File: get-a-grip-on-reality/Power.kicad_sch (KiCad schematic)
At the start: 16 parts, among them J1 Battery Connector, J4 Conn_01x05_Pin, U2 BQ25887

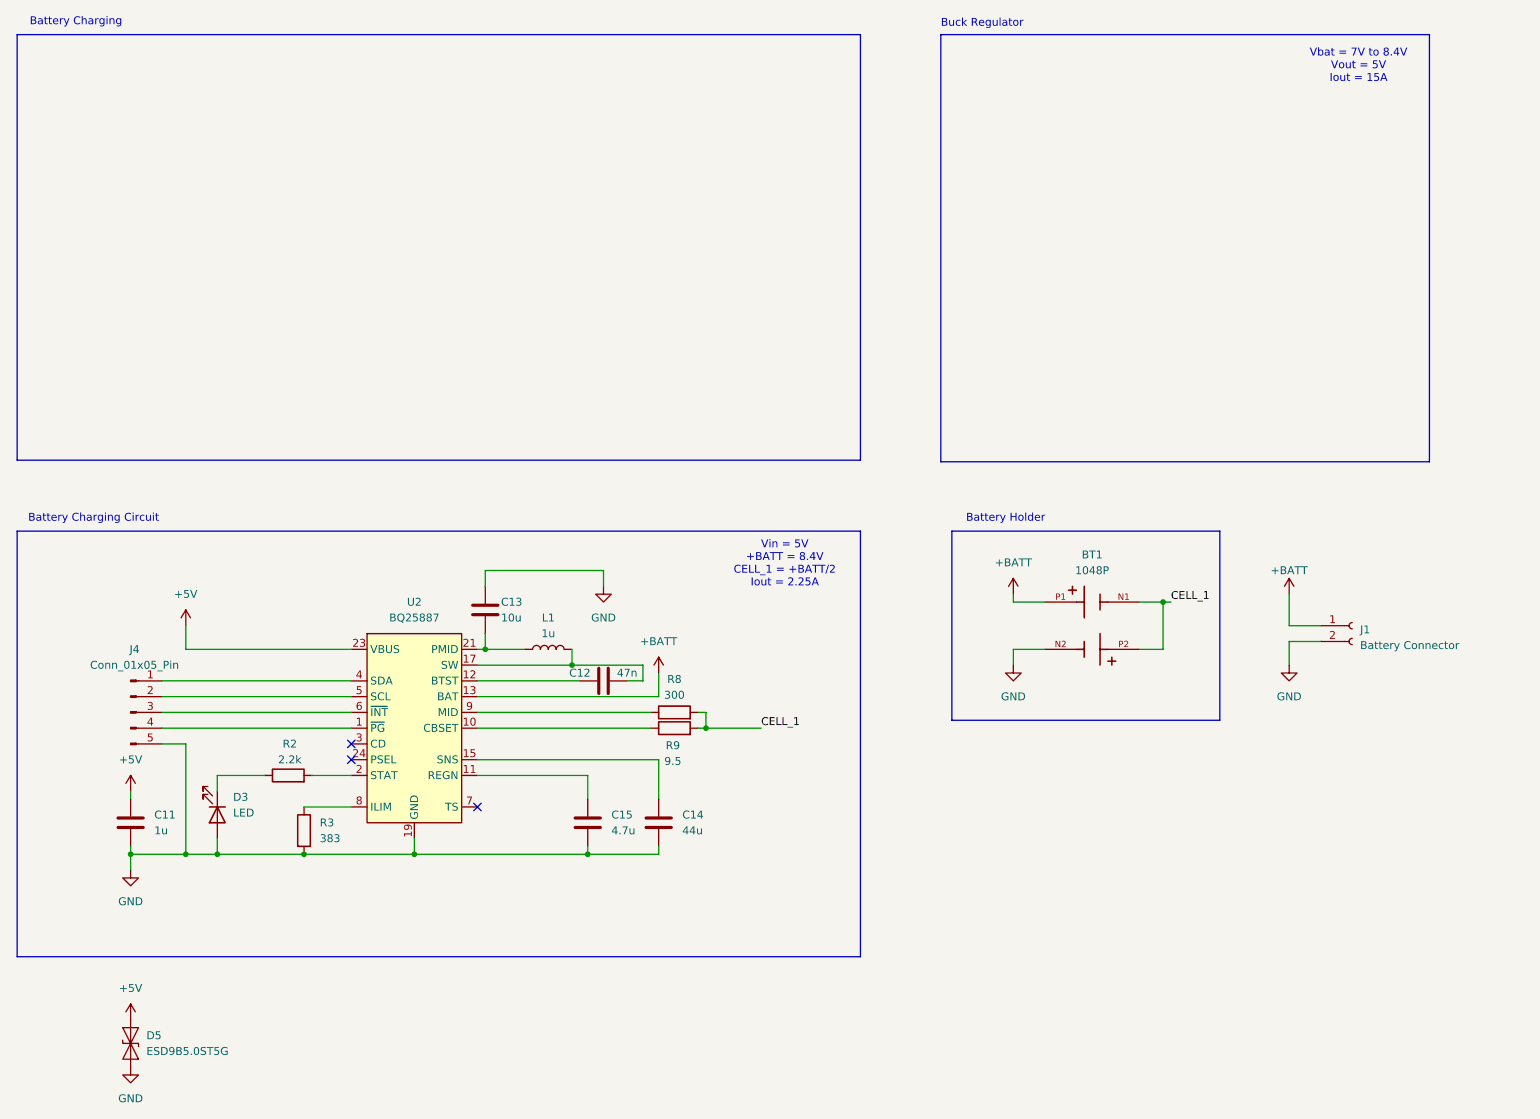
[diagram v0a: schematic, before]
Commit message: finish mcu and power page
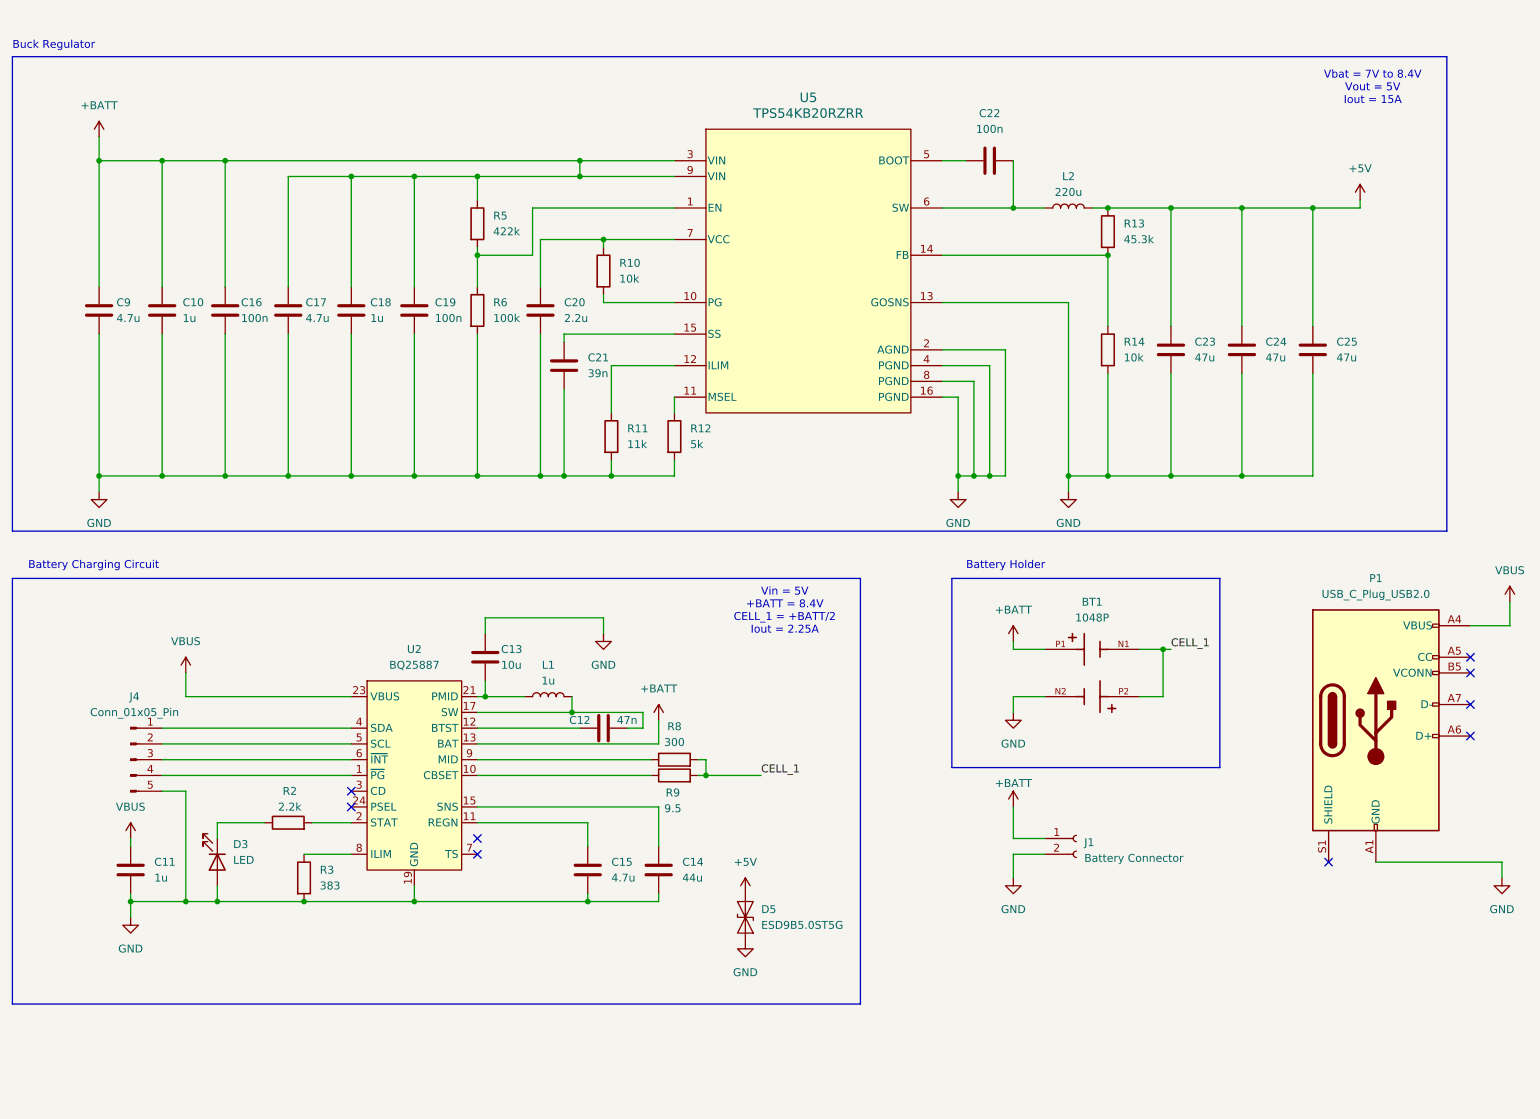
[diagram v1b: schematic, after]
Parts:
- added C10, C18: 1u, symbol Device:C
- added C16, C19, C22: 100n, symbol Device:C
- added C17, C9: 4.7u, symbol Device:C
- added C20: 2.2u, symbol Device:C
- added C21: 39n, symbol Device:C
- added C23, C24, C25: 47u, symbol Device:C
- added L2: 220u, symbol Device:L
- added P1: USB_C_Plug_USB2.0, symbol Connector:USB_C_Plug_USB2.0
- added R10, R14: 10k, symbol Device:R
- added R11: 11k, symbol Device:R
- added R12: 5k, symbol Device:R
- added R13: 45.3k, symbol Device:R
- added R5: 422k, symbol Device:R
- added R6: 100k, symbol Device:R
- added U5: TPS54KB20RZRR, RZR0016A-MFG, symbol 2024-06-26_16-50-44:TPS54KB20RZRR
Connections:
- net +5V: now also C23.1, C24.1, C25.1, L2.2, R13.1; no longer C11.1, U2.23 (VBUS)
- net +BATT: now also C10.1, C16.1, C17.1, C18.1, C19.1, C9.1, R5.1, U5.3 (VIN), U5.9 (VIN)
- net GND: now also C10.2, C16.2, C17.2, C18.2, C19.2, C20.2, C21.2, C23.2, C24.2, C25.2, C9.2, P1.A1 (GND), P1.A12 (GND), P1.B1 (GND), P1.B12 (GND), R11.2, R12.2, R14.2, R6.2, U5.13 (GOSNS), U5.16 (PGND), U5.2 (AGND), U5.4 (PGND), U5.8 (PGND)
- new net: C21.1, U5.15 (SS)
- new net: R12.1, U5.11 (MSEL)
- new net: C22.2, L2.1, U5.6 (SW)
- new net: R11.1, U5.12 (ILIM)
- new net: R5.2, R6.1, U5.1 (EN)
- new net: C22.1, U5.5 (BOOT)
- new net: C20.1, R10.1, U5.7 (VCC)
- new net: R10.2, U5.10 (PG)
- new net: R13.2, R14.1, U5.14 (FB)
- new net VBUS: C11.1, P1.A4 (VBUS), P1.A9 (VBUS), P1.B4 (VBUS), P1.B9 (VBUS), U2.23 (VBUS)
- no-connect marks 3 -> 9
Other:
- note removed: "Battery Charging"
- moved on the sheet: BT1, C11, C12, C13, C14, C15, D3, J1, J4, L1, R2, R3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

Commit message: add output
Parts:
- removed P1: USB_C_Plug_USB2.0, symbol Connector:USB_C_Plug_USB2.0
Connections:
- no-connect marks 9 -> 4

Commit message: add more to pcb
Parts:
- BT1: footprint 1048P:BAT_1048P -> fydp library:BAT_1048P
- C12: renamed from C11; footprint (none) -> Capacitor_SMD:C_0805_2012Metric
- C13: renamed from C9; footprint (none) -> Capacitor_SMD:C_0805_2012Metric
- C14: renamed from C10; footprint (none) -> Capacitor_SMD:C_0805_2012Metric
- C15: renamed from C16; footprint (none) -> Capacitor_SMD:C_0805_2012Metric
- C16: renamed from C17; footprint (none) -> Capacitor_SMD:C_0805_2012Metric
- C17: renamed from C18; footprint (none) -> Capacitor_SMD:C_0805_2012Metric
- C18: renamed from C19; footprint (none) -> Capacitor_SMD:C_0805_2012Metric
- C19: renamed from C13; footprint (none) -> Capacitor_SMD:C_0805_2012Metric
- C20, C21: footprint (none) -> Capacitor_SMD:C_0805_2012Metric
- C22: renamed from C15; footprint (none) -> Capacitor_SMD:C_0805_2012Metric
- C23: renamed from C12; footprint (none) -> Capacitor_SMD:C_0805_2012Metric
- C24: renamed from C14; footprint (none) -> Capacitor_SMD:C_0805_2012Metric
- C25: renamed from C22; footprint (none) -> Capacitor_SMD:C_0805_2012Metric
- C26: renamed from C23; footprint (none) -> Capacitor_SMD:C_0805_2012Metric
- C27: renamed from C24; footprint (none) -> Capacitor_SMD:C_0805_2012Metric
- C28: renamed from C25; footprint (none) -> Capacitor_SMD:C_0805_2012Metric
- D4: renamed from D3; footprint (none) -> LED_SMD:LED_0805_2012Metric
- J13: renamed from J4; footprint (none) -> Connector_PinHeader_2.54mm:PinHeader_1x05_P2.54mm_Vertical
- J14: renamed from J1; value Battery Connector -> Battery Connector Bat; footprint Connector_JST:JST_PH_S2B-PH-K_1x02_P2.00mm_Horizontal -> Connector_AMASS:AMASS_XT30PW-F_1x02_P2.50mm_Horizontal
- L1: footprint (none) -> Inductor_SMD:L_Taiyo-Yuden_MD-2020
- L2: footprint (none) -> Inductor_SMD:L_Bourns_SRU5016_5.2x5.2mm
- R10: renamed from R12; footprint (none) -> Resistor_SMD:R_0805_2012Metric
- R11: renamed from R8; footprint (none) -> Resistor_SMD:R_0805_2012Metric
- R12: renamed from R9; footprint (none) -> Resistor_SMD:R_0805_2012Metric
- R13, R14: footprint (none) -> Resistor_SMD:R_0805_2012Metric
- R4: renamed from R2; footprint (none) -> Resistor_SMD:R_0805_2012Metric
- R5: renamed from R3; footprint (none) -> Resistor_SMD:R_0805_2012Metric
- R6: renamed from R5; footprint (none) -> Resistor_SMD:R_0805_2012Metric
- R7: renamed from R6; footprint (none) -> Resistor_SMD:R_0805_2012Metric
- R8: renamed from R10; footprint (none) -> Resistor_SMD:R_0805_2012Metric
- R9: renamed from R11; footprint (none) -> Resistor_SMD:R_0805_2012Metric
- U6: renamed from U5; footprint RZR0016A-MFG -> fydp library:RZR0016A-MFG
- renumbered U2 to U5
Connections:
- net +5V: now also J14.1 (Pin_1)
- net +BATT: no longer J14.1 (Pin_1)
- net at J13.1 (Pin_1): now also U5.1 (~{PG}); no longer U5.4 (SDA)
- net at J13.2 (Pin_2): now also U5.4 (SDA); no longer U5.5 (SCL)
- net at J13.3 (Pin_3): now also U5.5 (SCL); no longer U5.6 (~{INT})
- net at J13.4 (Pin_4): now also U5.6 (~{INT}); no longer U5.1 (~{PG})
- net SW_5: now reaches C25.2, L2.1, U6.6 (SW)
- net SNS: now reaches C24.1, U5.15 (SNS), U5.16 (SNS)
- net SW_BAT: now reaches C23.2, L1.2, U5.17 (SW), U5.18 (SW)
- net PMID: now reaches C19.2, L1.1, U5.21 (PMID), U5.22 (PMID)
- net BOOT: now reaches C25.1, U6.5 (BOOT)
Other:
- moved on the sheet: C19, C22, C24

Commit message: fix schematic with winstons suggestions
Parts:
- added R8: 5.23k, symbol Device:R
- added R9: 30.1k, symbol Device:R
- added TH1: 10k, symbol Device:Thermistor
- renumbered J13 to J14, J14 to J15, R8 to R10, R9 to R11, R10 to R12, R11 to R13, R12 to R14, R13 to R15, R14 to R16
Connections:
- net GND: now also R9.2, TH1.2
- net at C22.1, U5.11 (REGN): now also R8.1
- net at U5.7 (TS): now also R8.2, R9.1, TH1.1
- no-connect marks 4 -> 2
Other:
- moved on the sheet: C22, C24, D4, R4, R5

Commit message: finish top pcb
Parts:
- R12: renamed from R8; footprint (none) -> Resistor_SMD:R_0805_2012Metric
- R13: renamed from R9; footprint (none) -> Resistor_SMD:R_0805_2012Metric
- TH1: footprint (none) -> Resistor_SMD:R_0805_2012Metric
- renumbered C12 to C14, C13 to C15, C14 to C16, C15 to C17, C16 to C18, C17 to C19, C18 to C20, C19 to C21, C20 to C22, C21 to C23, C22 to C24, C23 to C25, C24 to C26, C25 to C27, C26 to C28, C27 to C29, C28 to C30, D4 to D7, D5 to D8, R6 to R10, R7 to R11, R10 to R14, R11 to R15, R12 to R16, R13 to R17, R14 to R18, R15 to R19, R16 to R20, R4 to R8, R5 to R9, U5 to U6, U6 to U7
